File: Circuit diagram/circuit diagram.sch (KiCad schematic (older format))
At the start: 130 parts

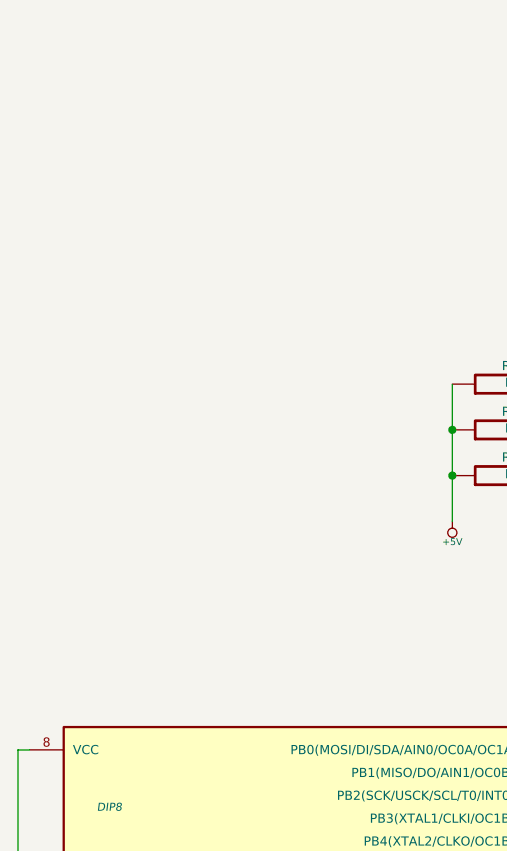
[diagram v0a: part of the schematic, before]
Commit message: Circuit diagram: add 7805 power supply
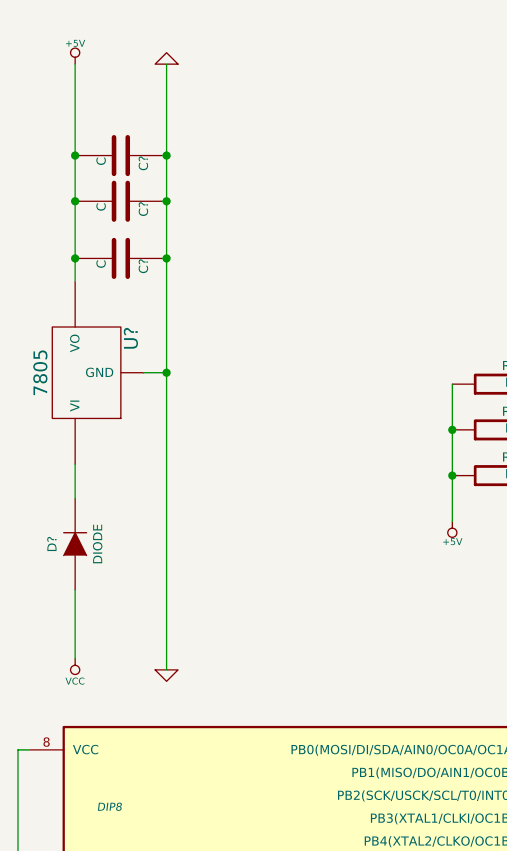
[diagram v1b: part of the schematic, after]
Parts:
- added C? (x3): C, symbol C
- added D?: DIODE, symbol DIODE
- added U?: 7805, symbol 7805
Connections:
- net +5V: now also C?.2, C?.2, C?.2, U?.VO
- net GND: now also C?.1, C?.1, C?.1, U?.GND
- net VCC: now also D?.1 (A)
- new net: D?.2 (K), U?.VI
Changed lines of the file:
@@
 LIBS:contrib
 LIBS:valves
-LIBS:Schaltplan-cache
-EELAYER 27 0
+LIBS:circuit diagram-cache
+EELAYER 25 0
 EELAYER END
 $Descr A4 11693 8268
@@
 Wire Wire Line
 	3650 3750 3450 3750
+$Comp
+L 7805 U?
+U 1 1 585C208D
+P 1000 2100
+F 0 "U?" H 1150 1904 60  0000 C CNN
+F 1 "7805" H 1000 2300 60  0000 C CNN
+F 2 "" H 1000 2100 60  0000 C CNN
+F 3 "" H 1000 2100 60  0000 C CNN
+	1    1000 2100
+	0    -1   -1   0
+$EndComp
+$Comp
+L C C?
+U 1 1 585C259A
+P 1150 1600
+F 0 "C?" H 1150 1700 40  0000 L CNN
+F 1 "C" H 1156 1515 40  0000 L CNN
+F 2 "" H 1188 1450 30  0000 C CNN
+F 3 "" H 1150 1600 60  0000 C CNN
+	1    1150 1600
+	0    1    1    0
+$EndComp
+$Comp
+L DIODE D?
+U 1 1 585C4801
+P 950 2850
+F 0 "D?" H 950 2950 40  0000 C CNN
+F 1 "DIODE" H 950 2750 40  0000 C CNN
+F 2 "" H 950 2850 60  0000 C CNN
+F 3 "" H 950 2850 60  0000 C CNN
+	1    950  2850
+	0    -1   -1   0
+$EndComp
+$Comp
+L C C?
+U 1 1 585C5E11
+P 1150 1150
+F 0 "C?" H 1150 1250 40  0000 L CNN
+F 1 "C" H 1156 1065 40  0000 L CNN
+F 2 "" H 1188 1000 30  0000 C CNN
+F 3 "" H 1150 1150 60  0000 C CNN
+	1    1150 1150
+	0    1    1    0
+$EndComp
+$Comp
+L C C?
+U 1 1 585C6072
+P 1150 1350
+F 0 "C?" H 1150 1450 40  0000 L CNN
+F 1 "C" H 1156 1265 40  0000 L CNN
+F 2 "" H 1188 1200 30  0000 C CNN
+F 3 "" H 1150 1350 60  0000 C CNN
+	1    1150 1350
+	0    1    1    0
+$EndComp
+Wire Wire Line
+	950  750  950  1700
+Connection ~ 950  1350
+Connection ~ 950  1600
+Wire Wire Line
+	1350 750  1350 3400
+Connection ~ 1350 1350
+Wire Wire Line
+	1350 2100 1250 2100
+Connection ~ 1350 1600
+Wire Wire Line
+	950  2500 950  2650
+$Comp
+L VCC #PWR?
+U 1 1 585C80C2
+P 950 3350
+F 0 "#PWR?" H 950 3450 30  0001 C CNN
+F 1 "VCC" H 950 3450 30  0000 C CNN
+F 2 "" H 950 3350 60  0001 C CNN
+F 3 "" H 950 3350 60  0001 C CNN
+	1    950  3350
+	-1   0    0    1
+$EndComp
+Wire Wire Line
+	950  3050 950  3350
+$Comp
+L GND #PWR?
+U 1 1 585C83E9
+P 1350 3400
+F 0 "#PWR?" H 1350 3400 30  0001 C CNN
+F 1 "GND" H 1350 3330 30  0001 C CNN
+F 2 "" H 1350 3400 60  0001 C CNN
+F 3 "" H 1350 3400 60  0001 C CNN
+	1    1350 3400
+	1    0    0    -1
+$EndComp
+Connection ~ 1350 2100
+$Comp
+L +5V #PWR?
+U 1 1 585CC1F6
+P 950 750
+F 0 "#PWR?" H 950 840 20  0001 C CNN
+F 1 "+5V" H 950 840 30  0000 C CNN
+F 2 "" H 950 750 60  0000 C CNN
+F 3 "" H 950 750 60  0000 C CNN
+	1    950  750
+	-1   0    0    -1
+$EndComp
+$Comp
+L GND #PWR?
+U 1 1 585CCC96
+P 1350 750
+F 0 "#PWR?" H 1350 750 30  0001 C CNN
+F 1 "GND" H 1350 680 30  0001 C CNN
+F 2 "" H 1350 750 60  0001 C CNN
+F 3 "" H 1350 750 60  0001 C CNN
+	1    1350 750
+	-1   0    0    1
+$EndComp
+Connection ~ 1350 1150
+Connection ~ 950  1150
 $EndSCHEMATC
